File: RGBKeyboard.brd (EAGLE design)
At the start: 96.5 x 94.9 mm, 35 parts

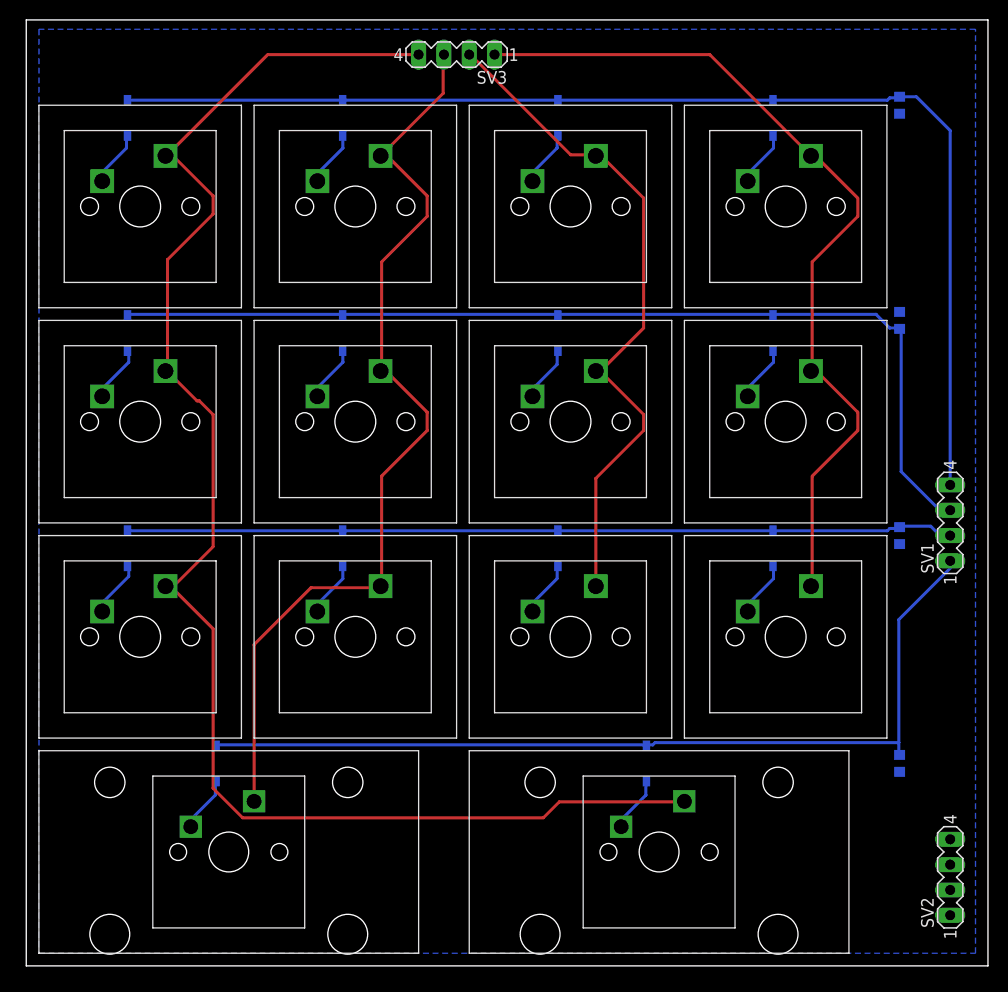
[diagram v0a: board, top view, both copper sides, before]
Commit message: Further reduce size by changing spacing
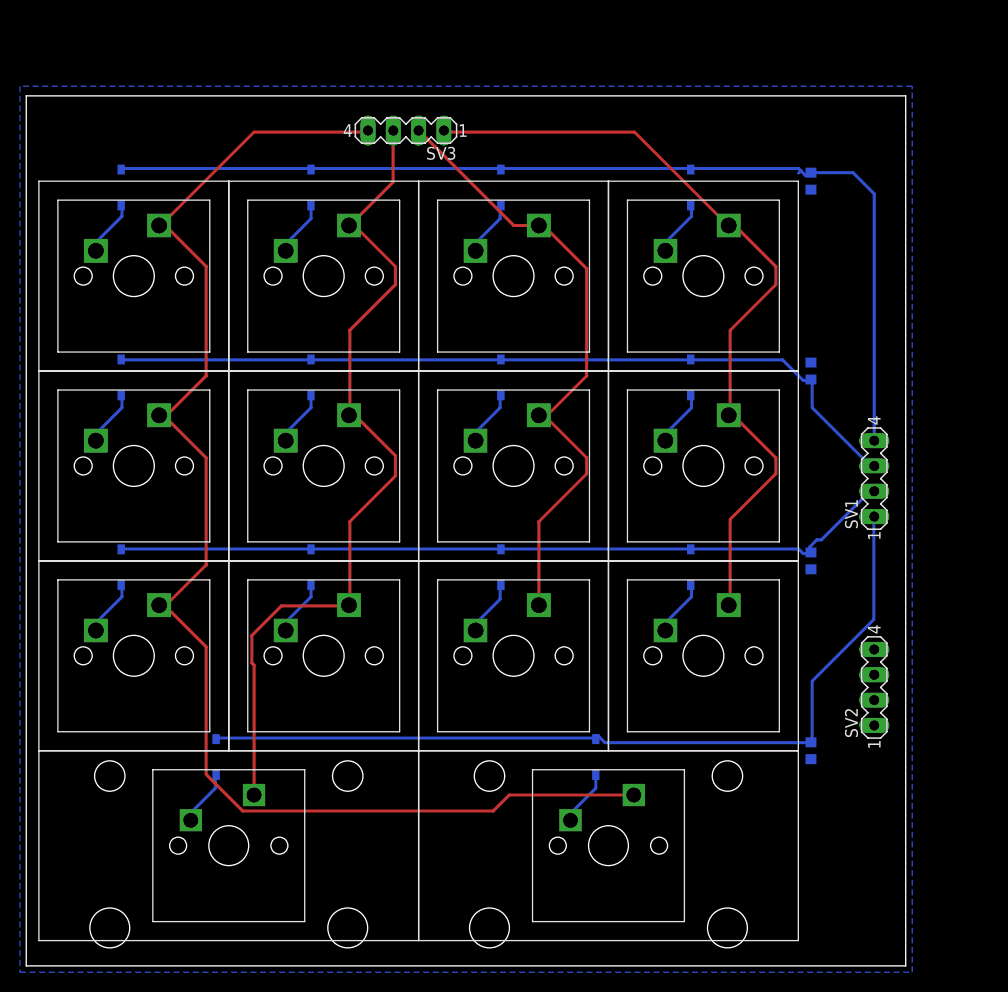
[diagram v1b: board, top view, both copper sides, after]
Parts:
- moved SV2 20.5 mm to (85.1, 27.9)
- moved R1 11.7 mm to (78.7, 78.7)
- moved D7 10.8 mm to (66.7, 78.1)
- moved U$12 10.8 mm to (67.9, 69.2)
- moved R2 10.2 mm to (78.7, 59.7)
- moved D9 9.38 mm to (66.7, 59.1)
- moved U$10 9.38 mm to (67.9, 50.2)
- moved R3 9.25 mm to (78.7, 40.6)
- moved SV3 9.16 mm to (38.1, 83.8)
- moved D6 9.03 mm to (47.6, 78.1)
- moved U$7 9.03 mm to (48.9, 69.2)
- moved R4 8.98 mm to (78.7, 21.6)
- moved SV1 8.82 mm to (85.1, 48.9)
- moved U$11 8.47 mm to (67.9, 31.1)
- moved D13 8.47 mm to (66.7, 40.0)
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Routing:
- net ROW0: track 119.9 -> 102.4 mm
- net ROW1: track 99.2 -> 81.8 mm
- net COL0: track 153.9 -> 137.0 mm
- net COL1: track 95.8 -> 85.2 mm
- net COL3: track 87.5 -> 79.1 mm
- net COL2: track 69.1 -> 63.3 mm
- net ROW3: track 90.3 -> 86.0 mm
- net ROW2: track 83.2 -> 78.9 mm
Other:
- board size 96.5 x 94.9 mm -> 88.2 x 87.3 mm
